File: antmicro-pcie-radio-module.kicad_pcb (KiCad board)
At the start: 4 copper layers, 80.2 x 22.1 mm, 134 parts, among them J1 MM8130-2600RA2, J2 2X05, J3 M.2-M+B-Pins, SW1 PTS840_GK_SMTR_LFS, U1 UPD720202, U2 SST25VF512A, U3 CoralAccelerator, U4 NRF52840, U5 TPS61232DRCR, U6 NCP380HMUAJAATBG, U7 TLV62568PDRLT, Y1 NX3225SA-24M, Y2 ABM11W-101-32.0000MHZ-T3, Y3 ABS06-32.768KHZ-9-1-T

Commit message: Add changes after pre-production review.
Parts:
- added C67: C_100n_0402, antmicro-pcie-radio-module-footprints:0402-cap, F.Cu at (153.1, 102.3)
- added C68: C_100n_0402, antmicro-pcie-radio-module-footprints:0402-cap, F.Cu at (150.2, 102.2)
- added C69: C_100n_0402, antmicro-pcie-radio-module-footprints:0402-cap, F.Cu at (146.5, 101.2)
- added R36: R_100k_0402, antmicro-pcie-radio-module-footprints:0402-res, F.Cu at (153.1, 101.2)
- added R37: R_8k2_0402, antmicro-pcie-radio-module-footprints:0402-res, B.Cu at (141.2, 103.2)
- added R38: R_10k_0402, antmicro-pcie-radio-module-footprints:0402-res, F.Cu at (149.2, 101.2)
- added R39: R_0R_0805, antmicro-pcie-radio-module-footprints:0805-res, F.Cu at (173.1, 106.0)
- added SW2: PTS840_GK_SMTR_LFS, antmicro-pcie-radio-module-footprints:CK-PTS840_GK_SMTR_LFS-0, F.Cu at (172.8, 93.2)
- added TP11: TP_SMD1MM, antmicro-pcie-radio-module-footprints:Testpoint_smd_1mm, B.Cu at (139.4, 92.7)
- added TP12: TP_SMD1MM, antmicro-pcie-radio-module-footprints:Testpoint_smd_1mm, B.Cu at (138.1, 92.8)
- added TP16: TP_SMD1MM, antmicro-pcie-radio-module-footprints:Testpoint_smd_1mm, B.Cu at (135.9, 92.1)
- added TP17: TP_SMD1MM, antmicro-pcie-radio-module-footprints:Testpoint_smd_1mm, F.Cu at (134.8, 92.2)
- added TP18: TP_SMD1MM, antmicro-pcie-radio-module-footprints:Testpoint_smd_1mm, F.Cu at (133.7, 92.3)
- added TP19: TP_SMD1MM, antmicro-pcie-radio-module-footprints:Testpoint_smd_1mm, F.Cu at (132.5, 92.3)
- added TP23: TP_SMD1MM, antmicro-pcie-radio-module-footprints:Testpoint_smd_1mm, F.Cu at (138.1, 102.7)
- ANT1: footprint pcie-radio-module:Linx-ANT-2.45-CHP-T-MFG -> antmicro-pcie-radio-module-footprints:Linx-ANT-2.45-CHP-T-MFG
- C1, C10, C11, C12, C13, C14, C15, C16, C17, C18, C19, C2, C20, C21, C22, C23, C24, C25, C26, C27, C28, C29, C3, C31, C32, C33, C34, C35, C36, C37, C38, C39, C4, C40, C41, C42, C43, C44, C45, C46, C47, C48, C49, C5, C50, C51, C52, C53, C54, C55, C56, C57, C59, C6, C62, C65, C7, C9: footprint pcie-radio-module:0402-cap -> antmicro-pcie-radio-module-footprints:0402-cap
- C30, C60, C63, C66, C8: footprint pcie-radio-module:0805-cap -> antmicro-pcie-radio-module-footprints:0805-cap
- C58, C61, C64: footprint pcie-radio-module:Panasonic_Electronic_Components-CD-0-0-MFG -> antmicro-pcie-radio-module-footprints:Panasonic_Electronic_Components-CD-0-0-MFG
- D1, D3, D4: footprint pcie-radio-module:LED0603 -> antmicro-pcie-radio-module-footprints:LED0603
- D2: footprint pcie-radio-module:LED_APHF1608LSEEQBDZGKC -> antmicro-pcie-radio-module-footprints:LED_APHF1608LSEEQBDZGKC
- FB1: footprint pcie-radio-module:0805-res -> antmicro-pcie-radio-module-footprints:0805-res
- J1: footprint pcie-radio-module:Murata-MM8130-2600RA2-MFG -> antmicro-pcie-radio-module-footprints:Murata-MM8130-2600RA2-MFG
- J2: footprint pcie-radio-module:ARM_SWD -> antmicro-pcie-radio-module-footprints:ARM_SWD
- J3: footprint pcie-radio-module:M.2-M+B-Keys -> antmicro-pcie-radio-module-footprints:M.2-M+B-Keys
- L1, L2: footprint pcie-radio-module:0603-res -> antmicro-pcie-radio-module-footprints:0603-res
- L3, L4, R1, R10, R11, R12, R13, R18, R2, R20, R21, R22, R29, R3, R33, R34, R35, R4, R5, R6, R7, R8, R9: footprint pcie-radio-module:0402-res -> antmicro-pcie-radio-module-footprints:0402-res
- L5: footprint pcie-radio-module:Coilcraft-XFL4020-0-0-MFG -> antmicro-pcie-radio-module-footprints:Coilcraft-XFL4020-0-0-MFG
- L6: footprint pcie-radio-module:Murata-DFE201610C-0-0-IPC_B -> antmicro-pcie-radio-module-footprints:Murata-DFE201610C-0-0-IPC_B
- MP1: footprint pcie-radio-module:M.2-Stud -> antmicro-pcie-radio-module-footprints:M.2-Stud
- N1: footprint pcie-radio-module:antmicro-logo_scaled_12mm -> antmicro-pcie-radio-module-footprints:antmicro-logo_scaled_12mm
- N2: footprint pcie-radio-module:OSHW-Logo2_7.3x6mm_Copper_Mask -> antmicro-pcie-radio-module-footprints:OSHW-Logo2_7.3x6mm_Copper_Mask
- R14, R16: value R_4k3_0402 -> R_8k2_0402; footprint antmicro-footprints:0402-res -> antmicro-pcie-radio-module-footprints:0402-res
- R15: value R_4k7_0402 -> R_10k_0402; footprint pcie-radio-module:0402-res -> antmicro-pcie-radio-module-footprints:0402-res
- R17, R19, R23, R24, R25, R26, R27, R28, R30, R32: footprint antmicro-footprints:0402-res -> antmicro-pcie-radio-module-footprints:0402-res
- R31: value R_0R_0402 -> R_10k_0402; footprint antmicro-footprints:0402-res -> antmicro-pcie-radio-module-footprints:0402-res
- SW1: footprint pcie-radio-module:CK-PTS840_GK_SMTR_LFS-0 -> antmicro-pcie-radio-module-footprints:CK-PTS840_GK_SMTR_LFS-0
- TP25, TP26, TP27, TP28: footprint antmicro-footprints:Testpoint_smd_1mm -> antmicro-pcie-radio-module-footprints:Testpoint_smd_1mm
- U1: footprint pcie-radio-module:QFN48-Renesas-UPD720202 -> antmicro-pcie-radio-module-footprints:QFN48-Renesas-UPD720202
- U2: footprint pcie-radio-module:SOIC8-SST25VF512A-33-4I-SAE-Level_B -> antmicro-pcie-radio-module-footprints:SOIC8-SST25VF512A-33-4I-SAE-Level_B
- U3: footprint pcie-radio-module:MODULE_G313-06329-00 -> antmicro-pcie-radio-module-footprints:MODULE_G313-06329-00
- U4: footprint pcie-radio-module:Nordic_Semiconductor-NRF52840-QIAA-R-0-0-MFG -> antmicro-pcie-radio-module-footprints:Nordic_Semiconductor-NRF52840-QIAA-R-0-0-MFG
- U5: footprint pcie-radio-module:VSON-10-1EP_3x3mm -> antmicro-pcie-radio-module-footprints:VSON-10-1EP_3x3mm
- U6: footprint pcie-radio-module:ON_Semiconductor-517AB-04_2013-C-IPC_B -> antmicro-pcie-radio-module-footprints:ON_Semiconductor-517AB-04_2013-C-IPC_B
- U7: footprint pcie-radio-module:SOT-563 -> antmicro-pcie-radio-module-footprints:SOT-563
- Y1: footprint pcie-radio-module:NDK-NX3225SA-0-0-MFG -> antmicro-pcie-radio-module-footprints:NDK-NX3225SA-0-0-MFG
- Y2: footprint pcie-radio-module:Abracon-ABM11W-0-0-0 -> antmicro-pcie-radio-module-footprints:Abracon-ABM11W-0-0-0
- Y3: footprint pcie-radio-module:Abracon-ABS06-32.768KHZ-T-0 -> antmicro-pcie-radio-module-footprints:Abracon-ABS06-32.768KHZ-T-0
- moved SW1 37.4 mm to (167.3, 93.3)
- moved D4 8.49 mm to (178.2, 92.5)
- moved R27 8.49 mm to (178.2, 93.6)
- moved R28 8.49 mm to (178.2, 92.6)
- moved D3 8.49 mm to (178.1, 93.6)
- moved R16 8.15 mm to (151.1, 101.3)
- moved N1 5.28 mm to (126.1, 106.5), turned to 90 degrees
- moved N2 5.01 mm to (120.1, 109.7), turned to 90 degrees
- moved L2 3.16 mm to (145.2, 92.9), turned to 90 degrees
- moved C36 2.73 mm to (141.6, 92.9), turned to 0 degrees
- moved TP27 2.56 mm to (176.3, 95.9)
- moved R17 1.94 mm to (148.0, 94.2)
- moved TP28 1.91 mm to (149.9, 93.2)
- moved C31 1.30 mm to (146.4, 94.7), turned to 270 degrees
- moved C32 1.12 mm to (147.0, 92.7)
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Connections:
- R14 pad 1: Net-(R14-Pad1) -> Net-(C69-Pad1)
- R15 pad 1: Net-(R14-Pad1) -> GND
- R15 pad 2: GND -> Net-(C69-Pad1)
- R31 pad 1: Net-(R31-Pad1) -> 3V3
- R31 pad 2: 3V3 -> Net-(R31-Pad2)
- U3 pad 53: CORAL_PMIC_EN -> Net-(R36-Pad2)
- U3 pad 76: Net-(R14-Pad1) -> Net-(C69-Pad1)
- U5 pad 9: Net-(R31-Pad1) -> Net-(R31-Pad2)
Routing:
- net /nRF52840/VDD: track 78.5 -> 39.0 mm, vias 10 -> 9
- net /nRF52840/~RESET: track 29.9 -> 62.5 mm, vias 2 -> 5
- net Net-(R31-Pad2): track 0.00 -> 31.5 mm, vias 0 -> 2
- net GND: track 56.6 -> 87.6 mm, vias 183 -> 205
- net Net-(R36-Pad2): track 0.00 -> 23.5 mm, vias 0 -> 2
- net CORAL_PMIC_EN: track 20.4 -> 4.09 mm, vias 2 -> 1
- net /powerSupply/3V3_PG: track 18.0 -> 26.9 mm
- net Net-(R16-Pad2): track 1.38 -> 10.1 mm
- net 3V3_CORAL: track 10.1 -> 18.8 mm
- net /powerSupply/1V05_PG: track 15.7 -> 7.26 mm
- net Net-(TP19-Pad1): track 0.00 -> 5.65 mm
- net Net-(TP23-Pad1): track 0.00 -> 4.90 mm
- net Net-(TP18-Pad1): track 0.00 -> 4.32 mm
- net Net-(TP17-Pad1): track 0.00 -> 3.75 mm
- net Net-(C69-Pad1): track 0.00 -> 3.29 mm
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- added copper zone on In2.Cu, net /nRF52840/VDD
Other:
- net class Default: clearance 0.1 -> 0.125
- rule trace_clearance: 0.1 -> 0.125
- rule trace_min: 0.12 -> 0.125
- rule via_min_drill: 0.3 -> 0.2
- board text added: "ePCI radio module rev 1.0.0 05/2021"
- board text added: "nRF.Brk"
- board text added: "nRF.RST"

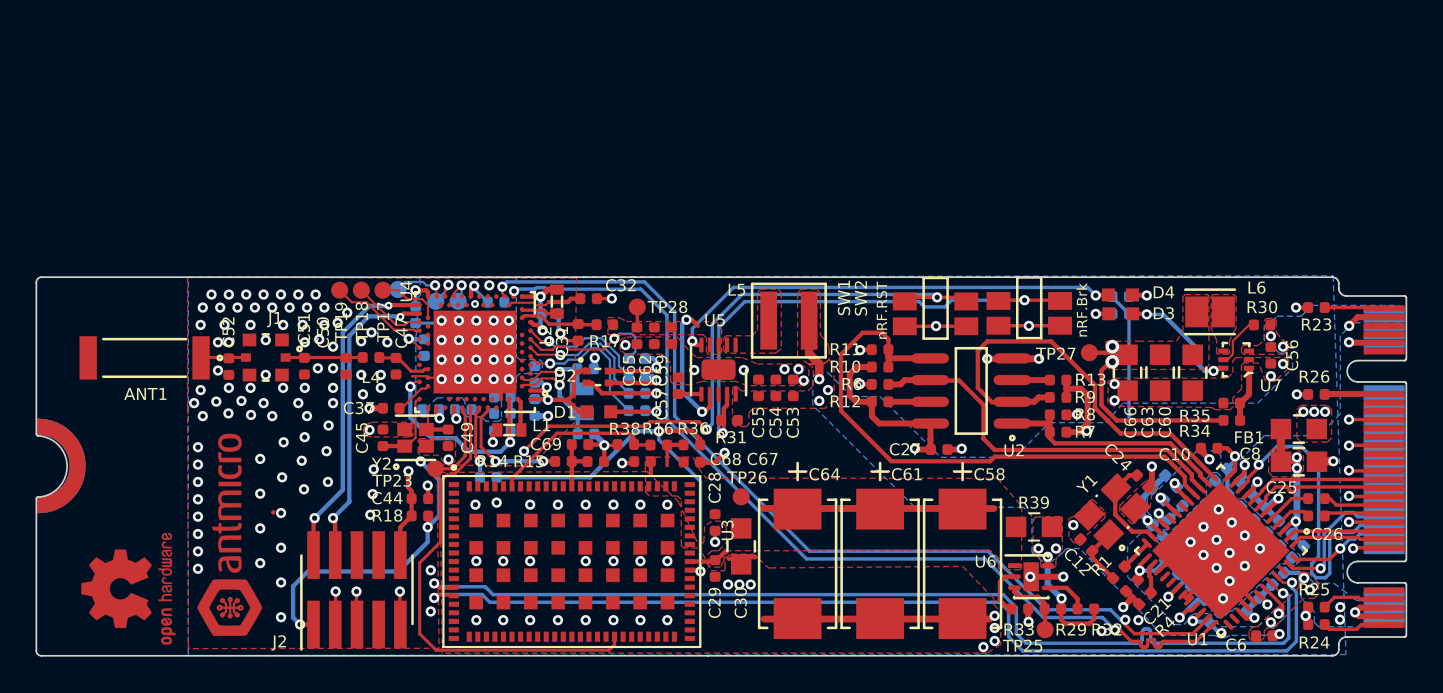
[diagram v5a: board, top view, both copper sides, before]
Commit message: Add BME280
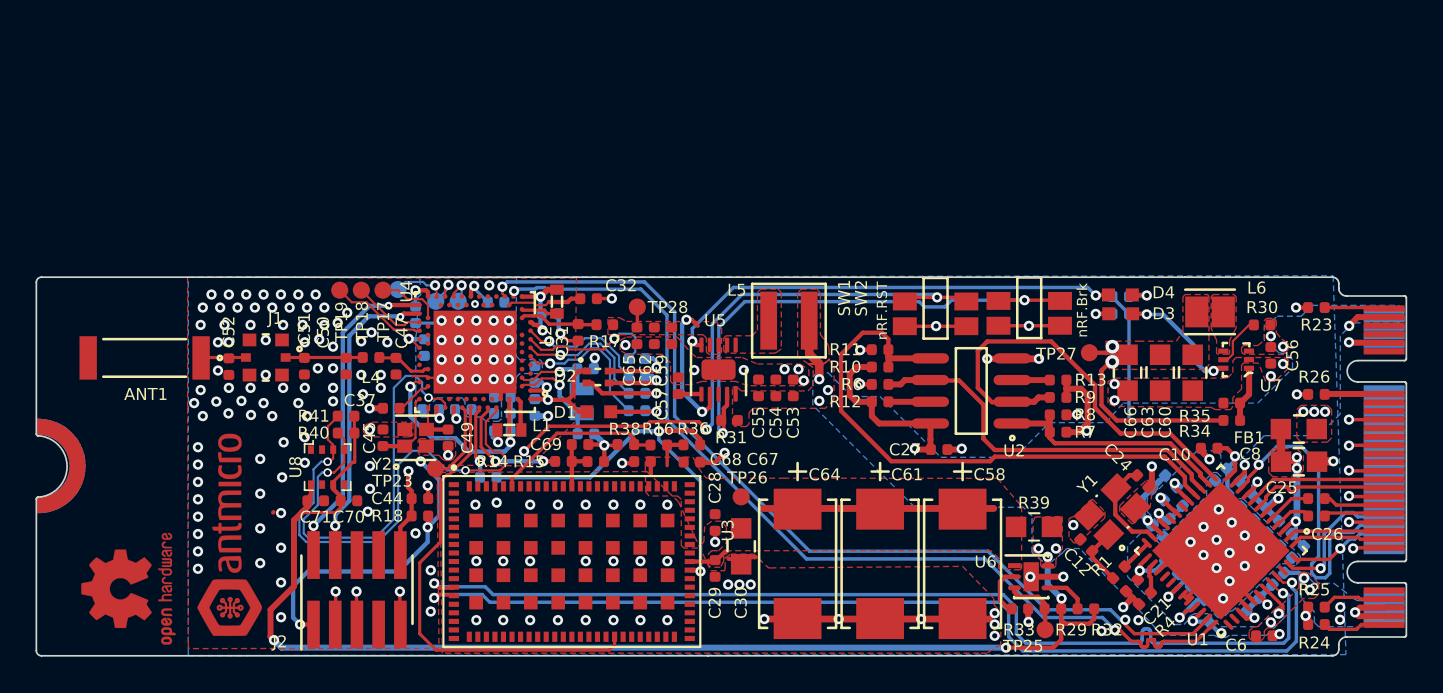
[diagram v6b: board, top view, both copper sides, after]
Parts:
- added C70: C_100n_0402, antmicro-pcie-radio-module-footprints:0402-cap, F.Cu at (133.0, 104.5)
- added C71: C_100n_0402, antmicro-pcie-radio-module-footprints:0402-cap, F.Cu at (131.1, 104.5)
- added R40: R_2k2_0402, antmicro-pcie-radio-module-footprints:0402-res, F.Cu at (132.8, 100.6)
- added R41: R_2k2_0402, antmicro-pcie-radio-module-footprints:0402-res, F.Cu at (132.8, 99.6)
- added U8: BME280, antmicro-footprints:Pressure_Sensor_LGA-8_2.5x2.5mm_BME280, F.Cu at (131.8, 102.6)
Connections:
- U4 pad A20: Net-(U4-PadA20) -> /nRF52840/SCL
- U4 pad A8: Net-(U4-PadA8) -> /nRF52840/SDA
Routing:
- net 3V3: track 51.4 -> 117.7 mm, vias 24 -> 26
- net /nRF52840/SDA: track 0.00 -> 29.8 mm, vias 0 -> 2
- net /nRF52840/SCL: track 0.00 -> 25.5 mm, vias 0 -> 2
- net GND: vias 205 -> 204
